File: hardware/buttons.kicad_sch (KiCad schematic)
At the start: 8 parts, among them SW1 C, SW2 D, SW3 E, SW4 F, SW5 G, SW6 A, SW7 H, SW8 OCTAVE?

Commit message: Update buttons.kicad_sch
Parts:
- SW1: footprint Button_Switch_SMD:SW_SPST_PTS647_Sx38 -> Button_Switch_THT:SW_TH_Tactile_Omron_B3F-100x
- SW2, SW3, SW4, SW5, SW6, SW7, SW8: footprint Button_Switch_SMD:SW_SPST_Omron_B3FS-100xP -> Button_Switch_THT:SW_TH_Tactile_Omron_B3F-100x
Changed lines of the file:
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@@
 			)
 		)
-		(property "Footprint" "Button_Switch_SMD:SW_SPST_Omron_B3FS-100xP"
+		(property "Footprint" "Button_Switch_THT:SW_TH_Tactile_Omron_B3F-100x"
 			(at 208.28 92.71 0)
 			(effects
@@
 			)
 		)
-		(property "Footprint" "Button_Switch_SMD:SW_SPST_Omron_B3FS-100xP"
+		(property "Footprint" "Button_Switch_THT:SW_TH_Tactile_Omron_B3F-100x"
 			(at 128.27 92.71 0)
 			(effects
@@
 			)
 		)
-		(property "Footprint" "Button_Switch_SMD:SW_SPST_Omron_B3FS-100xP"
+		(property "Footprint" "Button_Switch_THT:SW_TH_Tactile_Omron_B3F-100x"
 			(at 109.22 92.71 0)
 			(effects
@@
 			)
 		)
-		(property "Footprint" "Button_Switch_SMD:SW_SPST_Omron_B3FS-100xP"
+		(property "Footprint" "Button_Switch_THT:SW_TH_Tactile_Omron_B3F-100x"
 			(at 147.32 92.71 0)
 			(effects
@@
 			)
 		)
-		(property "Footprint" "Button_Switch_SMD:SW_SPST_Omron_B3FS-100xP"
+		(property "Footprint" "Button_Switch_THT:SW_TH_Tactile_Omron_B3F-100x"
 			(at 167.64 92.71 0)
 			(effects
@@
 			)
 		)
-		(property "Footprint" "Button_Switch_SMD:SW_SPST_PTS647_Sx38"
+		(property "Footprint" "Button_Switch_THT:SW_TH_Tactile_Omron_B3F-100x"
 			(at 71.12 92.71 0)
 			(effects
@@
 			)
 		)
-		(property "Footprint" "Button_Switch_SMD:SW_SPST_Omron_B3FS-100xP"
+		(property "Footprint" "Button_Switch_THT:SW_TH_Tactile_Omron_B3F-100x"
 			(at 187.96 92.71 0)
 			(effects
@@
 			)
 		)
-		(property "Footprint" "Button_Switch_SMD:SW_SPST_Omron_B3FS-100xP"
+		(property "Footprint" "Button_Switch_THT:SW_TH_Tactile_Omron_B3F-100x"
 			(at 90.17 92.71 0)
 			(effects

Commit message: minor schematic changes
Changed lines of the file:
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@@
 	(wire
 		(pts
-			(xy 152.4 72.39) (xy 152.4 97.79)
-		)
-		(stroke
-			(width 0)
-			(type default)
-		)
-	)
-	(wire
-		(pts
-			(xy 133.35 72.39) (xy 133.35 97.79)
+			(xy 152.4 62.23) (xy 152.4 97.79)
+		)
+		(stroke
+			(width 0)
+			(type default)
+		)
+	)
+	(wire
+		(pts
+			(xy 133.35 62.23) (xy 133.35 97.79)
 		)
 		(stroke
@@
 	(wire
 		(pts
-			(xy 76.2 72.39) (xy 76.2 97.79)
+			(xy 76.2 62.23) (xy 76.2 97.79)
 		)
 		(stroke
@@
 	(wire
 		(pts
-			(xy 213.36 72.39) (xy 213.36 97.79)
+			(xy 213.36 62.23) (xy 213.36 97.79)
 		)
 		(stroke
@@
 	(wire
 		(pts
-			(xy 193.04 72.39) (xy 193.04 97.79)
+			(xy 193.04 62.23) (xy 193.04 97.79)
 		)
 		(stroke
@@
 	(wire
 		(pts
-			(xy 114.3 72.39) (xy 114.3 97.79)
+			(xy 114.3 62.23) (xy 114.3 97.79)
 		)
 		(stroke
@@
 	(wire
 		(pts
-			(xy 95.25 72.39) (xy 95.25 97.79)
+			(xy 95.25 62.23) (xy 95.25 97.79)
 		)
 		(stroke
@@
 	(wire
 		(pts
-			(xy 172.72 72.39) (xy 172.72 97.79)
+			(xy 172.72 62.23) (xy 172.72 97.79)
 		)
 		(stroke
@@
 		)
 	)
-	(hierarchical_label "GPIO4"
-		(shape input)
-		(at 114.3 72.39 90)
-		(effects
-			(font
-				(size 1.27 1.27)
-				(thickness 0.254)
-				(bold yes)
-			)
-			(justify left)
-		)
-	)
-	(hierarchical_label "GPIO5"
-		(shape input)
-		(at 133.35 72.39 90)
-		(effects
-			(font
-				(size 1.27 1.27)
-				(thickness 0.254)
-				(bold yes)
-			)
-			(justify left)
-		)
-	)
-	(hierarchical_label "GPIO6"
-		(shape input)
-		(at 152.4 72.39 90)
-		(effects
-			(font
-				(size 1.27 1.27)
-				(thickness 0.254)
-				(bold yes)
-			)
-			(justify left)
-		)
-	)
-	(hierarchical_label "GPIO7"
-		(shape input)
-		(at 172.72 72.39 90)
-		(effects
-			(font
-				(size 1.27 1.27)
-				(thickness 0.254)
-				(bold yes)
-			)
-			(justify left)
-		)
-	)
-	(hierarchical_label "GPIO8"
-		(shape input)
-		(at 193.04 72.39 90)
-		(effects
-			(font
-				(size 1.27 1.27)
-				(thickness 0.254)
-				(bold yes)
-			)
-			(justify left)
-		)
-	)
-	(hierarchical_label "GPIO9"
-		(shape input)
-		(at 213.36 72.39 90)
-		(effects
-			(font
-				(size 1.27 1.27)
-				(thickness 0.254)
-				(bold yes)
-			)
-			(justify left)
-		)
-	)
-	(hierarchical_label "GPIO2"
-		(shape input)
-		(at 76.2 72.39 90)
-		(effects
-			(font
-				(size 1.27 1.27)
-				(thickness 0.254)
-				(bold yes)
-			)
-			(justify left)
-		)
-	)
-	(hierarchical_label "GPIO3"
-		(shape input)
-		(at 95.25 72.39 90)
-		(effects
-			(font
-				(size 1.27 1.27)
-				(thickness 0.254)
-				(bold yes)
-			)
-			(justify left)
-		)
-	)
+	(global_label "GPIO2"
+		(shape input)
+		(at 76.2 62.23 90)
+		(fields_autoplaced yes)
+		(effects
+			(font
+				(size 1.27 1.27)
+			)
+			(justify left)
+		)
+		(property "Intersheetrefs" "${INTERSHEET_REFS}"
+			(at 76.2 53.56 90)
+			(effects
+				(font
+					(size 1.27 1.27)
+				)
+				(justify left)
+				(hide yes)
+			)
+		)
+	)
+	(global_label "GPIO9"
+		(shape input)
+		(at 213.36 62.23 90)
+		(fields_autoplaced yes)
+		(effects
+			(font
+				(size 1.27 1.27)
+			)
+			(justify left)
+		)
+		(property "Intersheetrefs" "${INTERSHEET_REFS}"
+			(at 213.36 53.56 90)
+			(effects
+				(font
+					(size 1.27 1.27)
+				)
+				(justify left)
+				(hide yes)
+			)
+		)
+	)
+	(global_label "GPIO5"
+		(shape input)
+		(at 133.35 62.23 90)
+		(fields_autoplaced yes)
+		(effects
+			(font
+				(size 1.27 1.27)
+			)
+			(justify left)
+		)
+		(property "Intersheetrefs" "${INTERSHEET_REFS}"
+			(at 133.35 53.56 90)
+			(effects
+				(font
+					(size 1.27 1.27)
+				)
+				(justify left)
+				(hide yes)
+			)
+		)
+	)
+	(global_label "GPIO3"
+		(shape input)
+		(at 95.25 62.23 90)
+		(fields_autoplaced yes)
+		(effects
+			(font
+				(size 1.27 1.27)
+			)
+			(justify left)
+		)
+		(property "Intersheetrefs" "${INTERSHEET_REFS}"
+			(at 95.25 53.56 90)
+			(effects
+				(font
+					(size 1.27 1.27)
+				)
+				(justify left)
+				(hide yes)
+			)
+		)
+	)
+	(global_label "GPIO7"
+		(shape input)
+		(at 172.72 62.23 90)
+		(fields_autoplaced yes)
+		(effects
+			(font
+				(size 1.27 1.27)
+			)
+			(justify left)
+		)
+		(property "Intersheetrefs" "${INTERSHEET_REFS}"
+			(at 172.72 53.56 90)
+			(effects
+				(font
+					(size 1.27 1.27)
+				)
+				(justify left)
+				(hide yes)
+			)
+		)
+	)
+	(global_label "GPIO6"
+		(shape input)
+		(at 152.4 62.23 90)
+		(fields_autoplaced yes)
+		(effects
+			(font
+				(size 1.27 1.27)
+			)
+			(justify left)
+		)
+		(property "Intersheetrefs" "${INTERSHEET_REFS}"
+			(at 152.4 53.56 90)
+			(effects
+				(font
+					(size 1.27 1.27)
+				)
+				(justify left)
+				(hide yes)
+			)
+		)
+	)
+	(global_label "GPIO4"
+		(shape input)
+		(at 114.3 62.23 90)
+		(fields_autoplaced yes)
+		(effects
+			(font
+				(size 1.27 1.27)
+			)
+			(justify left)
+		)
+		(property "Intersheetrefs" "${INTERSHEET_REFS}"
+			(at 114.3 53.56 90)
+			(effects
+				(font
+					(size 1.27 1.27)
+				)
+				(justify left)
+				(hide yes)
+			)
+		)
+	)
+	(global_label "GPIO8"
+		(shape input)
+		(at 193.04 62.23 90)
+		(fields_autoplaced yes)
+		(effects
+			(font
+				(size 1.27 1.27)
+			)
+			(justify left)
+		)
+		(property "Intersheetrefs" "${INTERSHEET_REFS}"
+			(at 193.04 53.56 90)
+			(effects
+				(font
+					(size 1.27 1.27)
+				)
+				(justify left)
+				(hide yes)
+			)
+		)
+	)

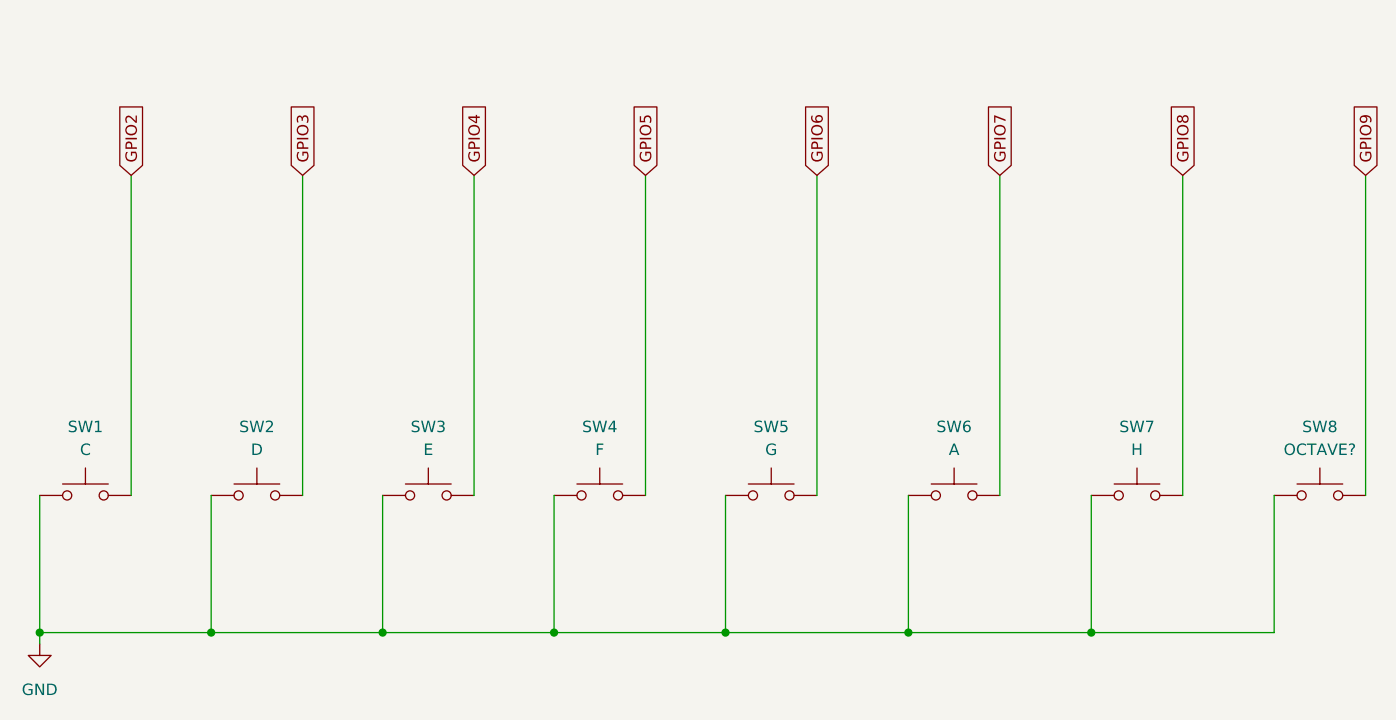
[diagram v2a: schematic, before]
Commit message: buttons added to the pcb
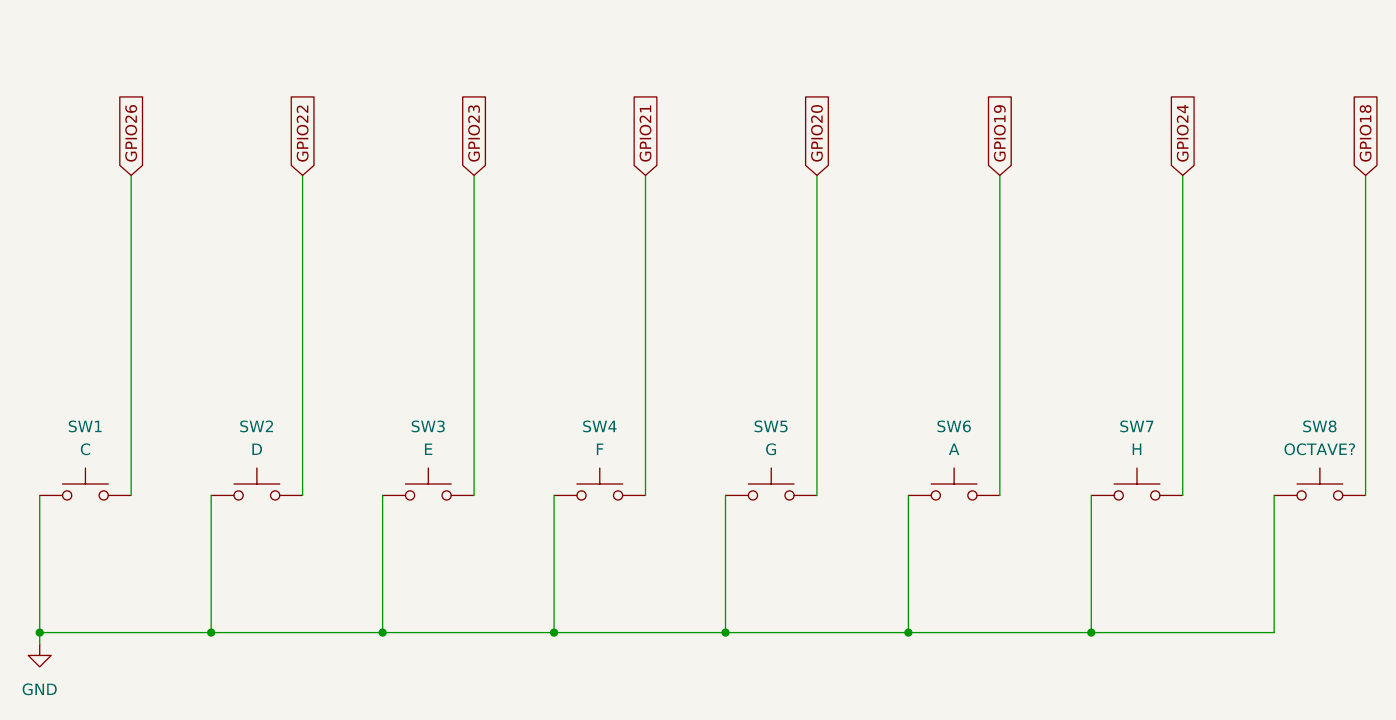
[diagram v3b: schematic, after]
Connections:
- net GPIO2 renamed GPIO26
- net GPIO3 renamed GPIO22
- net GPIO4 renamed GPIO23
- net GPIO5 renamed GPIO21
- net GPIO6 renamed GPIO20
- net GPIO7 renamed GPIO19
- net GPIO8 renamed GPIO24
- net GPIO9 renamed GPIO18
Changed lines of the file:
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@@
 		)
 	)
-	(global_label "GPIO2"
+	(global_label "GPIO26"
 		(shape input)
 		(at 76.2 62.23 90)
@@
 		)
 		(property "Intersheetrefs" "${INTERSHEET_REFS}"
-			(at 76.2 53.56 90)
+			(at 76.2 52.3505 90)
 			(effects
 				(font
@@
 		)
 	)
-	(global_label "GPIO9"
+	(global_label "GPIO18"
 		(shape input)
 		(at 213.36 62.23 90)
@@
 		)
 		(property "Intersheetrefs" "${INTERSHEET_REFS}"
-			(at 213.36 53.56 90)
+			(at 213.36 52.3505 90)
 			(effects
 				(font
@@
 		)
 	)
-	(global_label "GPIO5"
+	(global_label "GPIO21"
 		(shape input)
 		(at 133.35 62.23 90)
@@
 		)
 		(property "Intersheetrefs" "${INTERSHEET_REFS}"
-			(at 133.35 53.56 90)
+			(at 133.35 52.3505 90)
 			(effects
 				(font
@@
 		)
 	)
-	(global_label "GPIO3"
+	(global_label "GPIO22"
 		(shape input)
 		(at 95.25 62.23 90)
@@
 		)
 		(property "Intersheetrefs" "${INTERSHEET_REFS}"
-			(at 95.25 53.56 90)
+			(at 95.25 52.3505 90)
 			(effects
 				(font
@@
 		)
 	)
-	(global_label "GPIO7"
+	(global_label "GPIO19"
 		(shape input)
 		(at 172.72 62.23 90)
@@
 		)
 		(property "Intersheetrefs" "${INTERSHEET_REFS}"
-			(at 172.72 53.56 90)
+			(at 172.72 52.3505 90)
 			(effects
 				(font
@@
 		)
 	)
-	(global_label "GPIO6"
+	(global_label "GPIO20"
 		(shape input)
 		(at 152.4 62.23 90)
@@
 		)
 		(property "Intersheetrefs" "${INTERSHEET_REFS}"
-			(at 152.4 53.56 90)
+			(at 152.4 52.3505 90)
 			(effects
 				(font
@@
 		)
 	)
-	(global_label "GPIO4"
+	(global_label "GPIO23"
 		(shape input)
 		(at 114.3 62.23 90)
@@
 		)
 		(property "Intersheetrefs" "${INTERSHEET_REFS}"
-			(at 114.3 53.56 90)
+			(at 114.3 52.3505 90)
 			(effects
 				(font
@@
 		)
 	)
-	(global_label "GPIO8"
+	(global_label "GPIO24"
 		(shape input)
 		(at 193.04 62.23 90)
@@
 		)
 		(property "Intersheetrefs" "${INTERSHEET_REFS}"
-			(at 193.04 53.56 90)
+			(at 193.04 52.3505 90)
 			(effects
 				(font

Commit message: type of connections changed
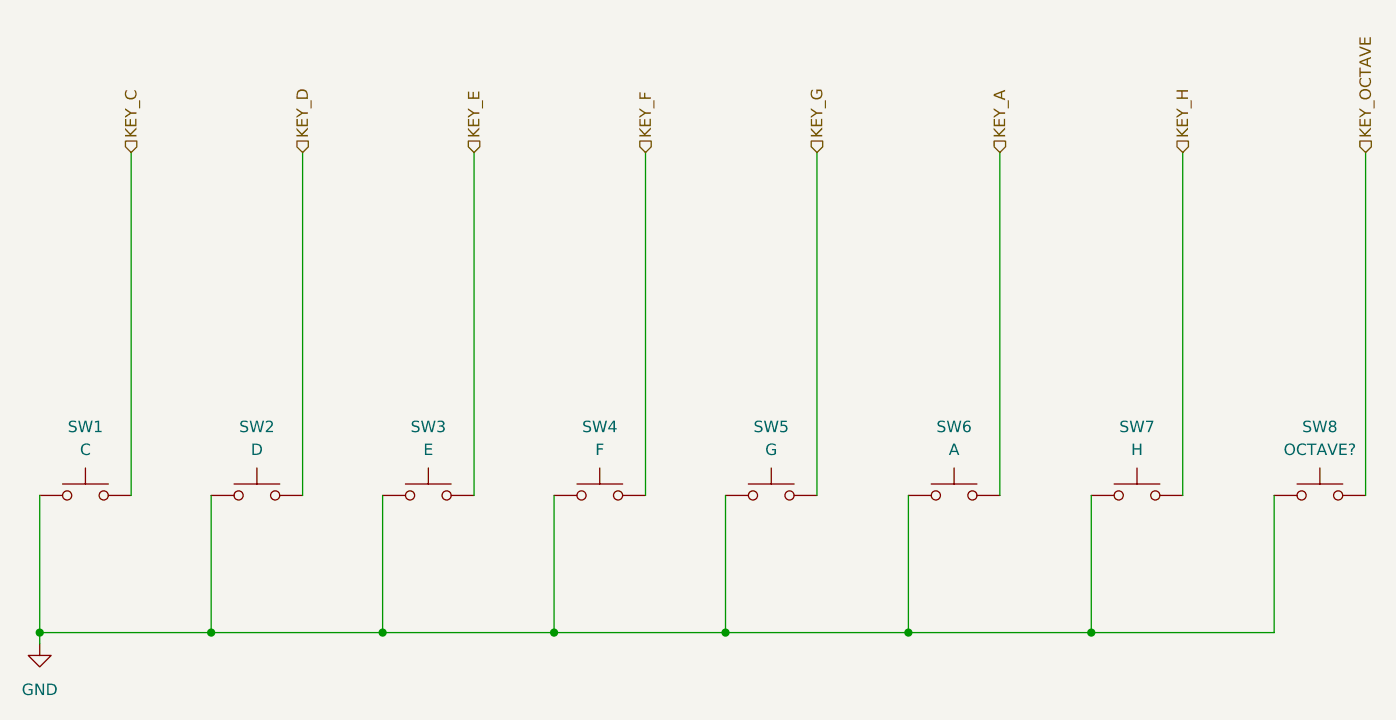
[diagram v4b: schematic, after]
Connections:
- net GPIO18 renamed KEY_OCTAVE
- net GPIO19 renamed KEY_A
- net GPIO20 renamed KEY_G
- net GPIO21 renamed KEY_F
- net GPIO22 renamed KEY_D
- net GPIO23 renamed KEY_E
- net GPIO24 renamed KEY_H
- net GPIO26 renamed KEY_C
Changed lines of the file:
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@@
 	(wire
 		(pts
-			(xy 152.4 62.23) (xy 152.4 97.79)
-		)
-		(stroke
-			(width 0)
-			(type default)
-		)
-	)
-	(wire
-		(pts
-			(xy 133.35 62.23) (xy 133.35 97.79)
+			(xy 152.4 59.69) (xy 152.4 97.79)
+		)
+		(stroke
+			(width 0)
+			(type default)
+		)
+	)
+	(wire
+		(pts
+			(xy 133.35 59.69) (xy 133.35 97.79)
 		)
 		(stroke
@@
 	(wire
 		(pts
-			(xy 76.2 62.23) (xy 76.2 97.79)
+			(xy 76.2 59.69) (xy 76.2 97.79)
 		)
 		(stroke
@@
 	(wire
 		(pts
-			(xy 213.36 62.23) (xy 213.36 97.79)
+			(xy 213.36 59.69) (xy 213.36 97.79)
 		)
 		(stroke
@@
 	(wire
 		(pts
-			(xy 193.04 62.23) (xy 193.04 97.79)
+			(xy 193.04 59.69) (xy 193.04 97.79)
 		)
 		(stroke
@@
 	(wire
 		(pts
-			(xy 114.3 62.23) (xy 114.3 97.79)
+			(xy 114.3 59.69) (xy 114.3 97.79)
 		)
 		(stroke
@@
 	(wire
 		(pts
-			(xy 95.25 62.23) (xy 95.25 97.79)
+			(xy 95.25 59.69) (xy 95.25 97.79)
 		)
 		(stroke
@@
 	(wire
 		(pts
-			(xy 172.72 62.23) (xy 172.72 97.79)
+			(xy 172.72 59.69) (xy 172.72 97.79)
 		)
 		(stroke
@@
 		)
 	)
-	(global_label "GPIO26"
-		(shape input)
-		(at 76.2 62.23 90)
-		(fields_autoplaced yes)
-		(effects
-			(font
-				(size 1.27 1.27)
-			)
-			(justify left)
-		)
-		(property "Intersheetrefs" "${INTERSHEET_REFS}"
-			(at 76.2 52.3505 90)
-			(effects
-				(font
-					(size 1.27 1.27)
-				)
-				(justify left)
-				(hide yes)
-			)
-		)
-	)
-	(global_label "GPIO18"
-		(shape input)
-		(at 213.36 62.23 90)
-		(fields_autoplaced yes)
-		(effects
-			(font
-				(size 1.27 1.27)
-			)
-			(justify left)
-		)
-		(property "Intersheetrefs" "${INTERSHEET_REFS}"
-			(at 213.36 52.3505 90)
-			(effects
-				(font
-					(size 1.27 1.27)
-				)
-				(justify left)
-				(hide yes)
-			)
-		)
-	)
-	(global_label "GPIO21"
-		(shape input)
-		(at 133.35 62.23 90)
-		(fields_autoplaced yes)
-		(effects
-			(font
-				(size 1.27 1.27)
-			)
-			(justify left)
-		)
-		(property "Intersheetrefs" "${INTERSHEET_REFS}"
-			(at 133.35 52.3505 90)
-			(effects
-				(font
-					(size 1.27 1.27)
-				)
-				(justify left)
-				(hide yes)
-			)
-		)
-	)
-	(global_label "GPIO22"
-		(shape input)
-		(at 95.25 62.23 90)
-		(fields_autoplaced yes)
-		(effects
-			(font
-				(size 1.27 1.27)
-			)
-			(justify left)
-		)
-		(property "Intersheetrefs" "${INTERSHEET_REFS}"
-			(at 95.25 52.3505 90)
-			(effects
-				(font
-					(size 1.27 1.27)
-				)
-				(justify left)
-				(hide yes)
-			)
-		)
-	)
-	(global_label "GPIO19"
-		(shape input)
-		(at 172.72 62.23 90)
-		(fields_autoplaced yes)
-		(effects
-			(font
-				(size 1.27 1.27)
-			)
-			(justify left)
-		)
-		(property "Intersheetrefs" "${INTERSHEET_REFS}"
-			(at 172.72 52.3505 90)
-			(effects
-				(font
-					(size 1.27 1.27)
-				)
-				(justify left)
-				(hide yes)
-			)
-		)
-	)
-	(global_label "GPIO20"
-		(shape input)
-		(at 152.4 62.23 90)
-		(fields_autoplaced yes)
-		(effects
-			(font
-				(size 1.27 1.27)
-			)
-			(justify left)
-		)
-		(property "Intersheetrefs" "${INTERSHEET_REFS}"
-			(at 152.4 52.3505 90)
-			(effects
-				(font
-					(size 1.27 1.27)
-				)
-				(justify left)
-				(hide yes)
-			)
-		)
-	)
-	(global_label "GPIO23"
-		(shape input)
-		(at 114.3 62.23 90)
-		(fields_autoplaced yes)
-		(effects
-			(font
-				(size 1.27 1.27)
-			)
-			(justify left)
-		)
-		(property "Intersheetrefs" "${INTERSHEET_REFS}"
-			(at 114.3 52.3505 90)
-			(effects
-				(font
-					(size 1.27 1.27)
-				)
-				(justify left)
-				(hide yes)
-			)
-		)
-	)
-	(global_label "GPIO24"
-		(shape input)
-		(at 193.04 62.23 90)
-		(fields_autoplaced yes)
-		(effects
-			(font
-				(size 1.27 1.27)
-			)
-			(justify left)
-		)
-		(property "Intersheetrefs" "${INTERSHEET_REFS}"
-			(at 193.04 52.3505 90)
-			(effects
-				(font
-					(size 1.27 1.27)
-				)
-				(justify left)
-				(hide yes)
-			)
-		)
-	)
+	(hierarchical_label "KEY_E"
+		(shape input)
+		(at 114.3 59.69 90)
+		(effects
+			(font
+				(size 1.27 1.27)
+			)
+			(justify left)
+		)
+	)
+	(hierarchical_label "KEY_F"
+		(shape input)
+		(at 133.35 59.69 90)
+		(effects
+			(font
+				(size 1.27 1.27)
+			)
+			(justify left)
+		)
+	)
+	(hierarchical_label "KEY_C"
+		(shape input)
+		(at 76.2 59.69 90)
+		(effects
+			(font
+				(size 1.27 1.27)
+			)
+			(justify left)
+		)
+	)
+	(hierarchical_label "KEY_G"
+		(shape input)
+		(at 152.4 59.69 90)
+		(effects
+			(font
+				(size 1.27 1.27)
+			)
+			(justify left)
+		)
+	)
+	(hierarchical_label "KEY_H"
+		(shape input)
+		(at 193.04 59.69 90)
+		(effects
+			(font
+				(size 1.27 1.27)
+			)
+			(justify left)
+		)
+	)
+	(hierarchical_label "KEY_OCTAVE"
+		(shape input)
+		(at 213.36 59.69 90)
+		(effects
+			(font
+				(size 1.27 1.27)
+			)
+			(justify left)
+		)
+	)
+	(hierarchical_label "KEY_A"
+		(shape input)
+		(at 172.72 59.69 90)
+		(effects
+			(font
+				(size 1.27 1.27)
+			)
+			(justify left)
+		)
+	)
+	(hierarchical_label "KEY_D"
+		(shape input)
+		(at 95.25 59.69 90)
+		(effects
+			(font
+				(size 1.27 1.27)
+			)
+			(justify left)
+		)
+	)
